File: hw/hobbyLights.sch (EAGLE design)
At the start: 62 parts, among them Q1 BC857BSMD, Q2 BC857BSMD, U1 MCP73831-2, U2 POWER, U3 BD48K28G, U4 ATMEGA32U4-AU, U5 TPS61222, Y1 RESONATORSMD

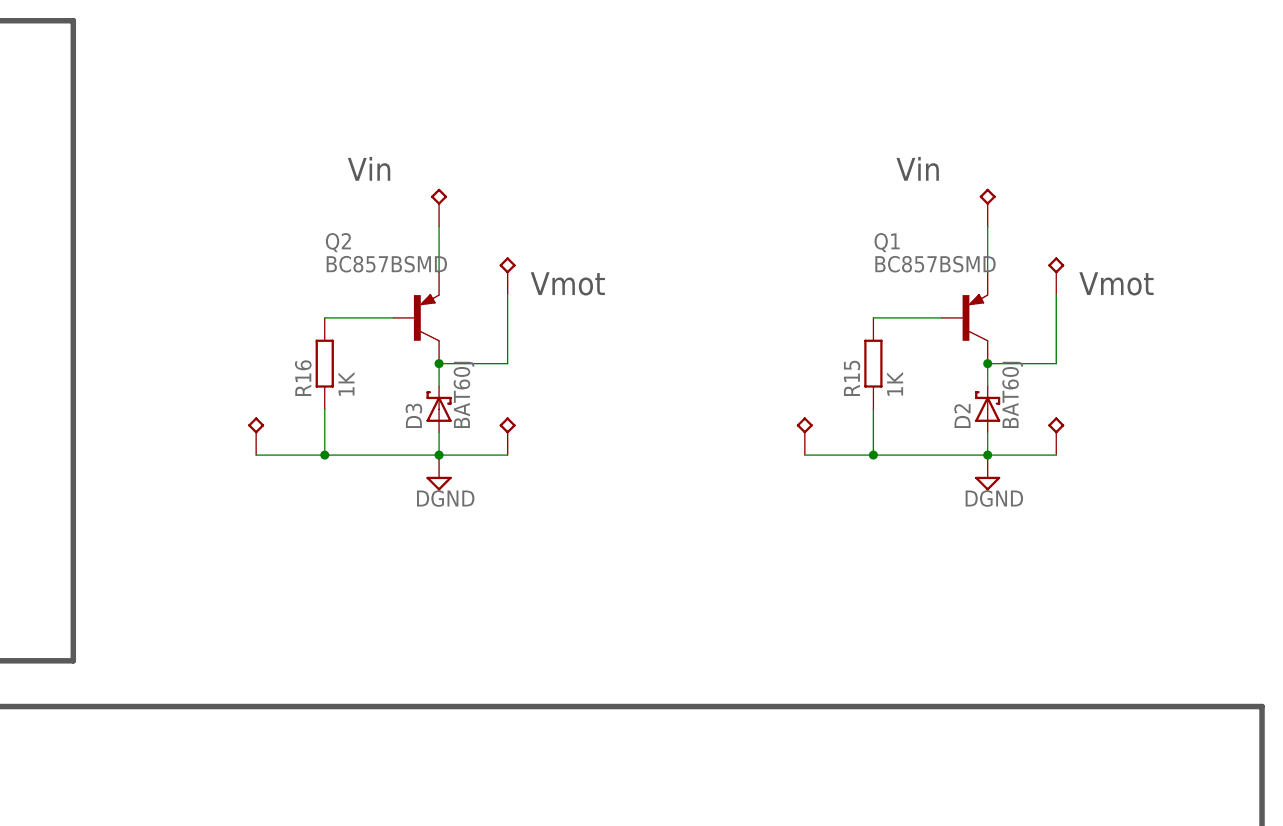
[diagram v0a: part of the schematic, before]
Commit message: Updated diodes and added frames.
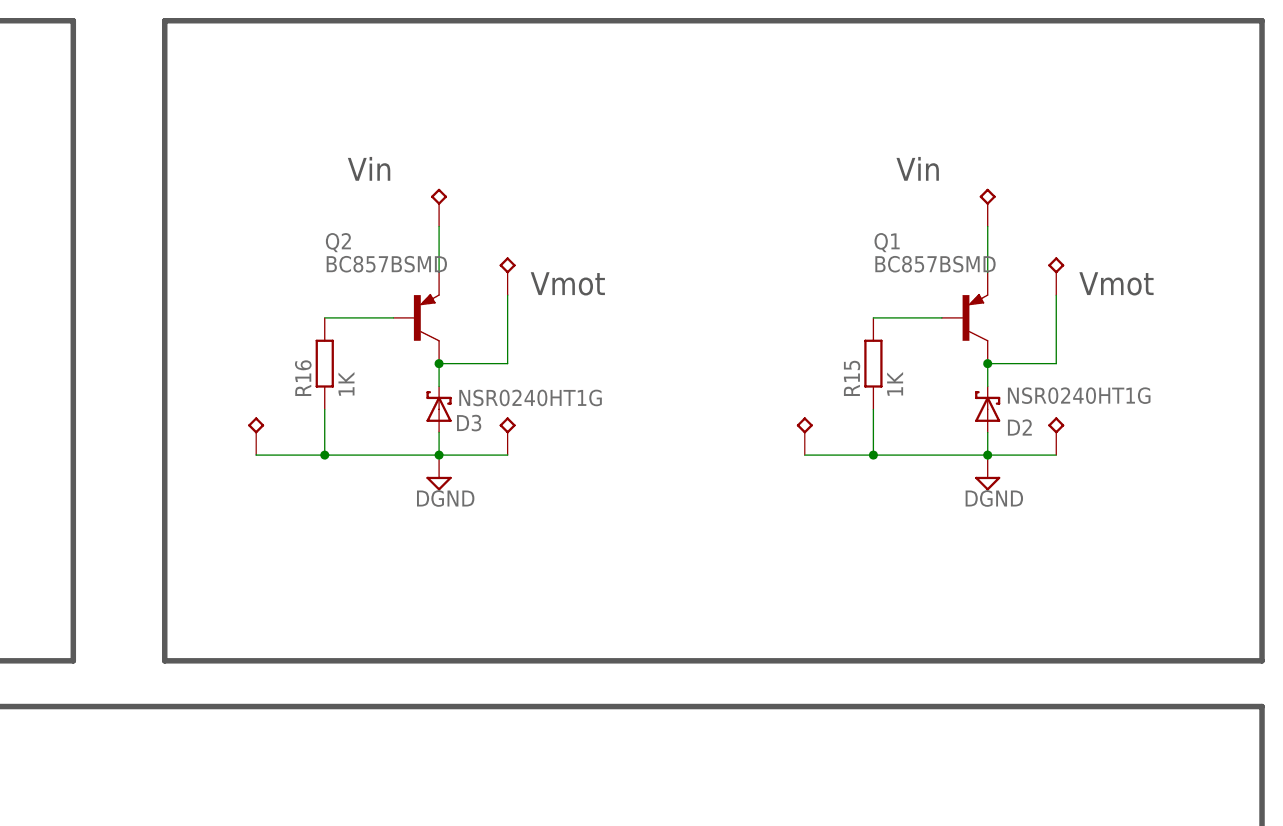
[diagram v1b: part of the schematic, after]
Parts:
- D2, D3: value BAT60J -> NSR0240HT1G
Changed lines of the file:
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@@
 <part name="SUPPLY8" library="supply2" deviceset="DGND" device=""/>
 <part name="R15" library="rcl" deviceset="R-EU_" device="R0603" value="1K"/>
-<part name="D2" library="diode" deviceset="BAT60J" device=""/>
+<part name="D2" library="diode" deviceset="BAT60J" device="" value="NSR0240HT1G"/>
 <part name="U$12" library="fmc" deviceset="TP_3X2" device=""/>
 <part name="U$13" library="fmc" deviceset="TP_3X2" device=""/>
@@
 <part name="SUPPLY9" library="supply2" deviceset="DGND" device=""/>
 <part name="R16" library="rcl" deviceset="R-EU_" device="R0603" value="1K"/>
-<part name="D3" library="diode" deviceset="BAT60J" device=""/>
+<part name="D3" library="diode" deviceset="BAT60J" device="" value="NSR0240HT1G"/>
 <part name="U$14" library="fmc" deviceset="TP_3X2" device=""/>
 <part name="U$15" library="fmc" deviceset="TP_3X2" device=""/>
@@
 <text x="299.72" y="228.6" size="2.54" layer="97" ratio="12">Vmot</text>
 <text x="279.4" y="241.3" size="2.54" layer="97" ratio="12">Vin</text>
+<wire x1="381" y1="259.08" x2="259.08" y2="259.08" width="0.6096" layer="97"/>
+<wire x1="259.08" y1="187.96" x2="259.08" y2="259.08" width="0.6096" layer="97"/>
+<wire x1="259.08" y1="187.96" x2="381" y2="187.96" width="0.6096" layer="97"/>
+<wire x1="381" y1="187.96" x2="381" y2="259.08" width="0.6096" layer="97"/>
 </plain>
 <instances>
@@
 <instance part="SUPPLY8" gate="G$1" x="350.52" y="208.28"/>
 <instance part="R15" gate="G$1" x="337.82" y="220.98" rot="R90"/>
-<instance part="D2" gate="G$1" x="350.52" y="215.9" rot="R90"/>
+<instance part="D2" gate="G$1" x="350.52" y="215.9" smashed="yes" rot="R90">
+<attribute name="NAME" x="352.552" y="212.979" size="1.778" layer="95"/>
+<attribute name="VALUE" x="352.552" y="216.535" size="1.778" layer="96"/>
+</instance>
 <instance part="U$12" gate="G$1" x="330.2" y="213.36" rot="R90"/>
 <instance part="U$13" gate="G$1" x="358.14" y="213.36" rot="R90"/>
@@
 <instance part="SUPPLY9" gate="G$1" x="289.56" y="208.28"/>
 <instance part="R16" gate="G$1" x="276.86" y="220.98" rot="R90"/>
-<instance part="D3" gate="G$1" x="289.56" y="215.9" rot="R90"/>
+<instance part="D3" gate="G$1" x="289.56" y="215.9" smashed="yes" rot="R90">
+<attribute name="NAME" x="291.338" y="213.487" size="1.778" layer="95"/>
+<attribute name="VALUE" x="291.592" y="216.281" size="1.778" layer="96"/>
+</instance>
 <instance part="U$14" gate="G$1" x="269.24" y="213.36" rot="R90"/>
 <instance part="U$15" gate="G$1" x="297.18" y="213.36" rot="R90"/>

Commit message: Removed side boards.
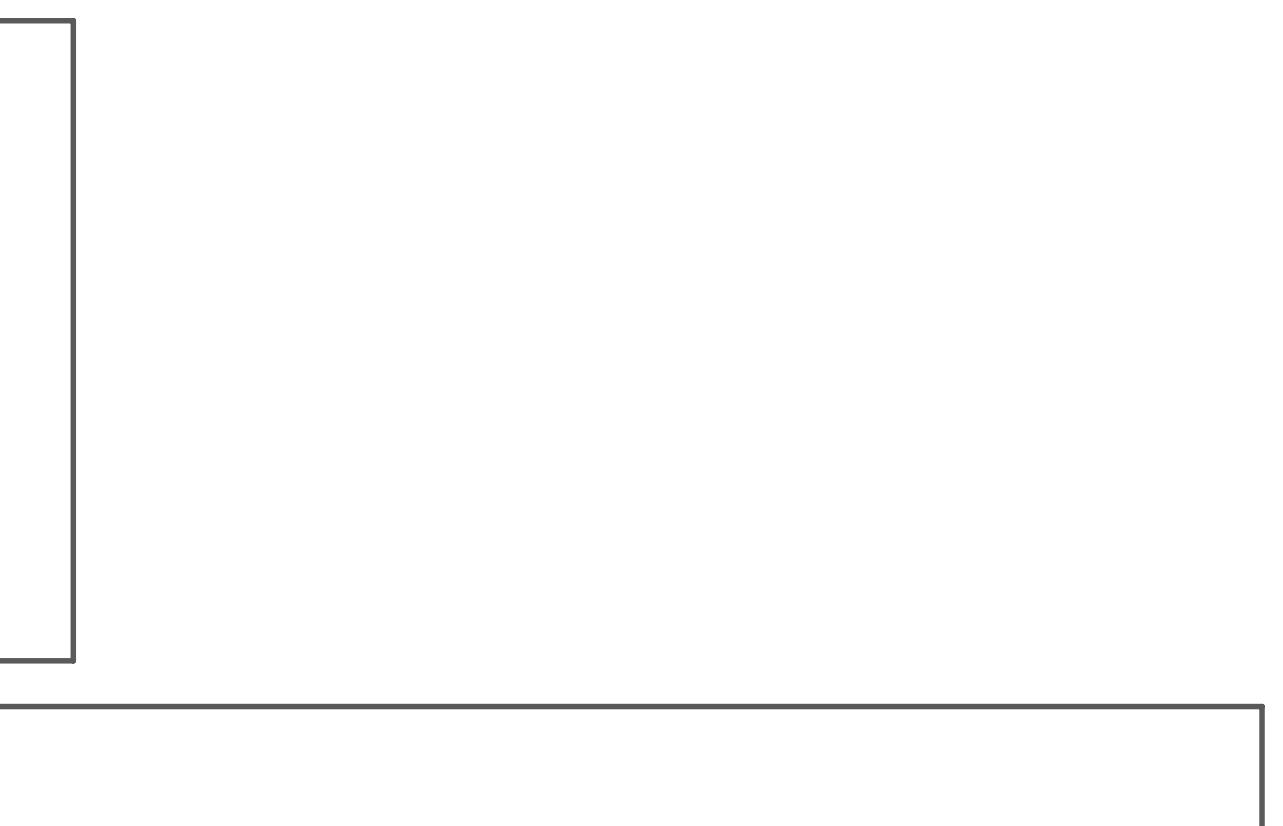
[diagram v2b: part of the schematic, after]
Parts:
- removed D2, D3: NSR0240HT1G, diode:BAT60J
- removed MOT, MOT1, U$12, U$13, U$14, U$15, VIN, VIN1: TP_3X2, fmc:TP_3X2
- removed Q1, Q2: BC857BSMD, transistor-pnp:BC857BSMD
- removed R15, R16: 1K, rcl:R-EU_R0603
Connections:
- removed net DGND: D2.A, D3.A, R15.1, R16.1, U$12.TP1, U$13.TP1, U$14.TP1, U$15.TP1
- removed net N$1: Q1.B, R15.2
- removed net N$11: Q1.E, VIN.TP1
- removed net N$24: Q2.B, R16.2
- removed net N$25: D3.C, MOT1.TP1, Q2.C
- removed net N$26: Q2.E, VIN1.TP1
- removed net N$8: D2.C, MOT.TP1, Q1.C
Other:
- note removed: "Vin"
- note removed: "Vmot"
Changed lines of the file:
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@@
 <part name="VCC2" library="supply1" deviceset="VCCINT" device=""/>
 <part name="SUPPLY7" library="SparkFun-Aesthetics" deviceset="V_BATT" device="" value="V_IN"/>
-<part name="Q1" library="transistor-pnp" deviceset="BC857*" device="SMD" technology="B"/>
-<part name="SUPPLY8" library="supply2" deviceset="DGND" device=""/>
-<part name="R15" library="rcl" deviceset="R-EU_" device="R0603" value="1K"/>
-<part name="D2" library="diode" deviceset="BAT60J" device="" value="NSR0240HT1G"/>
-<part name="U$12" library="fmc" deviceset="TP_3X2" device=""/>
-<part name="U$13" library="fmc" deviceset="TP_3X2" device=""/>
-<part name="MOT" library="fmc" deviceset="TP_3X2" device=""/>
-<part name="VIN" library="fmc" deviceset="TP_3X2" device=""/>
-<part name="Q2" library="transistor-pnp" deviceset="BC857*" device="SMD" technology="B"/>
-<part name="SUPPLY9" library="supply2" deviceset="DGND" device=""/>
-<part name="R16" library="rcl" deviceset="R-EU_" device="R0603" value="1K"/>
-<part name="D3" library="diode" deviceset="BAT60J" device="" value="NSR0240HT1G"/>
-<part name="U$14" library="fmc" deviceset="TP_3X2" device=""/>
-<part name="U$15" library="fmc" deviceset="TP_3X2" device=""/>
-<part name="MOT1" library="fmc" deviceset="TP_3X2" device=""/>
-<part name="VIN1" library="fmc" deviceset="TP_3X2" device=""/>
 </parts>
 <sheets>
@@
 <wire x1="154.94" y1="182.88" x2="218.44" y2="182.88" width="0.6096" layer="97"/>
 <wire x1="218.44" y1="182.88" x2="218.44" y2="43.18" width="0.6096" layer="97"/>
-<text x="360.68" y="228.6" size="2.54" layer="97" ratio="12">Vmot</text>
-<text x="340.36" y="241.3" size="2.54" layer="97" ratio="12">Vin</text>
-<text x="299.72" y="228.6" size="2.54" layer="97" ratio="12">Vmot</text>
-<text x="279.4" y="241.3" size="2.54" layer="97" ratio="12">Vin</text>
-<wire x1="381" y1="259.08" x2="259.08" y2="259.08" width="0.6096" layer="97"/>
-<wire x1="259.08" y1="187.96" x2="259.08" y2="259.08" width="0.6096" layer="97"/>
-<wire x1="259.08" y1="187.96" x2="381" y2="187.96" width="0.6096" layer="97"/>
-<wire x1="381" y1="187.96" x2="381" y2="259.08" width="0.6096" layer="97"/>
 </plain>
 <instances>
@@
 <instance part="VCC2" gate="G$1" x="96.52" y="30.48"/>
 <instance part="SUPPLY7" gate="G$1" x="121.92" y="99.06"/>
-<instance part="Q1" gate="G$1" x="347.98" y="226.06"/>
-<instance part="SUPPLY8" gate="G$1" x="350.52" y="208.28"/>
-<instance part="R15" gate="G$1" x="337.82" y="220.98" rot="R90"/>
-<instance part="D2" gate="G$1" x="350.52" y="215.9" smashed="yes" rot="R90">
-<attribute name="NAME" x="352.552" y="212.979" size="1.778" layer="95"/>
-<attribute name="VALUE" x="352.552" y="216.535" size="1.778" layer="96"/>
-</instance>
-<instance part="U$12" gate="G$1" x="330.2" y="213.36" rot="R90"/>
-<instance part="U$13" gate="G$1" x="358.14" y="213.36" rot="R90"/>
-<instance part="MOT" gate="G$1" x="358.14" y="231.14" rot="R90"/>
-<instance part="VIN" gate="G$1" x="350.52" y="238.76" rot="R90"/>
-<instance part="Q2" gate="G$1" x="287.02" y="226.06"/>
-<instance part="SUPPLY9" gate="G$1" x="289.56" y="208.28"/>
-<instance part="R16" gate="G$1" x="276.86" y="220.98" rot="R90"/>
-<instance part="D3" gate="G$1" x="289.56" y="215.9" smashed="yes" rot="R90">
-<attribute name="NAME" x="291.338" y="213.487" size="1.778" layer="95"/>
-<attribute name="VALUE" x="291.592" y="216.281" size="1.778" layer="96"/>
-</instance>
-<instance part="U$14" gate="G$1" x="269.24" y="213.36" rot="R90"/>
-<instance part="U$15" gate="G$1" x="297.18" y="213.36" rot="R90"/>
-<instance part="MOT1" gate="G$1" x="297.18" y="231.14" rot="R90"/>
-<instance part="VIN1" gate="G$1" x="289.56" y="238.76" rot="R90"/>
 </instances>
 <busses>
@@
 </segment>
 </net>
-<net name="DGND" class="0">
-<segment>
-<pinref part="SUPPLY8" gate="G$1" pin="DGND"/>
-<wire x1="330.2" y1="210.82" x2="337.82" y2="210.82" width="0.1524" layer="91"/>
-<wire x1="337.82" y1="210.82" x2="350.52" y2="210.82" width="0.1524" layer="91"/>
-<wire x1="350.52" y1="210.82" x2="358.14" y2="210.82" width="0.1524" layer="91"/>
-<junction x="350.52" y="210.82"/>
-<pinref part="R15" gate="G$1" pin="1"/>
-<wire x1="337.82" y1="215.9" x2="337.82" y2="210.82" width="0.1524" layer="91"/>
-<junction x="337.82" y="210.82"/>
-<pinref part="D2" gate="G$1" pin="A"/>
-<wire x1="350.52" y1="213.36" x2="350.52" y2="210.82" width="0.1524" layer="91"/>
-<pinref part="U$12" gate="G$1" pin="TP1"/>
-<pinref part="U$13" gate="G$1" pin="TP1"/>
-</segment>
-<segment>
-<pinref part="SUPPLY9" gate="G$1" pin="DGND"/>
-<wire x1="269.24" y1="210.82" x2="276.86" y2="210.82" width="0.1524" layer="91"/>
-<wire x1="276.86" y1="210.82" x2="289.56" y2="210.82" width="0.1524" layer="91"/>
-<wire x1="289.56" y1="210.82" x2="297.18" y2="210.82" width="0.1524" layer="91"/>
-<junction x="289.56" y="210.82"/>
-<pinref part="R16" gate="G$1" pin="1"/>
-<wire x1="276.86" y1="215.9" x2="276.86" y2="210.82" width="0.1524" layer="91"/>
-<junction x="276.86" y="210.82"/>
-<pinref part="D3" gate="G$1" pin="A"/>
-<wire x1="289.56" y1="213.36" x2="289.56" y2="210.82" width="0.1524" layer="91"/>
-<pinref part="U$14" gate="G$1" pin="TP1"/>
-<pinref part="U$15" gate="G$1" pin="TP1"/>
-</segment>
-</net>
-<net name="N$1" class="0">
-<segment>
-<pinref part="Q1" gate="G$1" pin="B"/>
-<pinref part="R15" gate="G$1" pin="2"/>
-<wire x1="345.44" y1="226.06" x2="337.82" y2="226.06" width="0.1524" layer="91"/>
-</segment>
-</net>
-<net name="N$8" class="0">
-<segment>
-<wire x1="358.14" y1="228.6" x2="358.14" y2="220.98" width="0.1524" layer="91"/>
-<pinref part="Q1" gate="G$1" pin="C"/>
-<wire x1="358.14" y1="220.98" x2="350.52" y2="220.98" width="0.1524" layer="91"/>
-<pinref part="D2" gate="G$1" pin="C"/>
-<wire x1="350.52" y1="218.44" x2="350.52" y2="220.98" width="0.1524" layer="91"/>
-<junction x="350.52" y="220.98"/>
-<pinref part="MOT" gate="G$1" pin="TP1"/>
-</segment>
-</net>
-<net name="N$11" class="0">
-<segment>
-<pinref part="Q1" gate="G$1" pin="E"/>
-<wire x1="350.52" y1="236.22" x2="350.52" y2="231.14" width="0.1524" layer="91"/>
-<pinref part="VIN" gate="G$1" pin="TP1"/>
-</segment>
-</net>
-<net name="N$24" class="0">
-<segment>
-<pinref part="Q2" gate="G$1" pin="B"/>
-<pinref part="R16" gate="G$1" pin="2"/>
-<wire x1="284.48" y1="226.06" x2="276.86" y2="226.06" width="0.1524" layer="91"/>
-</segment>
-</net>
-<net name="N$25" class="0">
-<segment>
-<wire x1="297.18" y1="228.6" x2="297.18" y2="220.98" width="0.1524" layer="91"/>
-<pinref part="Q2" gate="G$1" pin="C"/>
-<wire x1="297.18" y1="220.98" x2="289.56" y2="220.98" width="0.1524" layer="91"/>
-<pinref part="D3" gate="G$1" pin="C"/>
-<wire x1="289.56" y1="218.44" x2="289.56" y2="220.98" width="0.1524" layer="91"/>
-<junction x="289.56" y="220.98"/>
-<pinref part="MOT1" gate="G$1" pin="TP1"/>
-</segment>
-</net>
-<net name="N$26" class="0">
-<segment>
-<pinref part="Q2" gate="G$1" pin="E"/>
-<wire x1="289.56" y1="236.22" x2="289.56" y2="231.14" width="0.1524" layer="91"/>
-<pinref part="VIN1" gate="G$1" pin="TP1"/>
-</segment>
-</net>
